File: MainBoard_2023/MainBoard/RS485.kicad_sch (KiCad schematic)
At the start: 26 parts, among them J8 43223-6113, U10 LTC1480CN8#PBF, U11 MAX3485, U12 LTC1480CN8#PBF, U13 MAX3485, U14 LTC1480CN8#PBF, U8 MAX3485, U9 TC7S14F

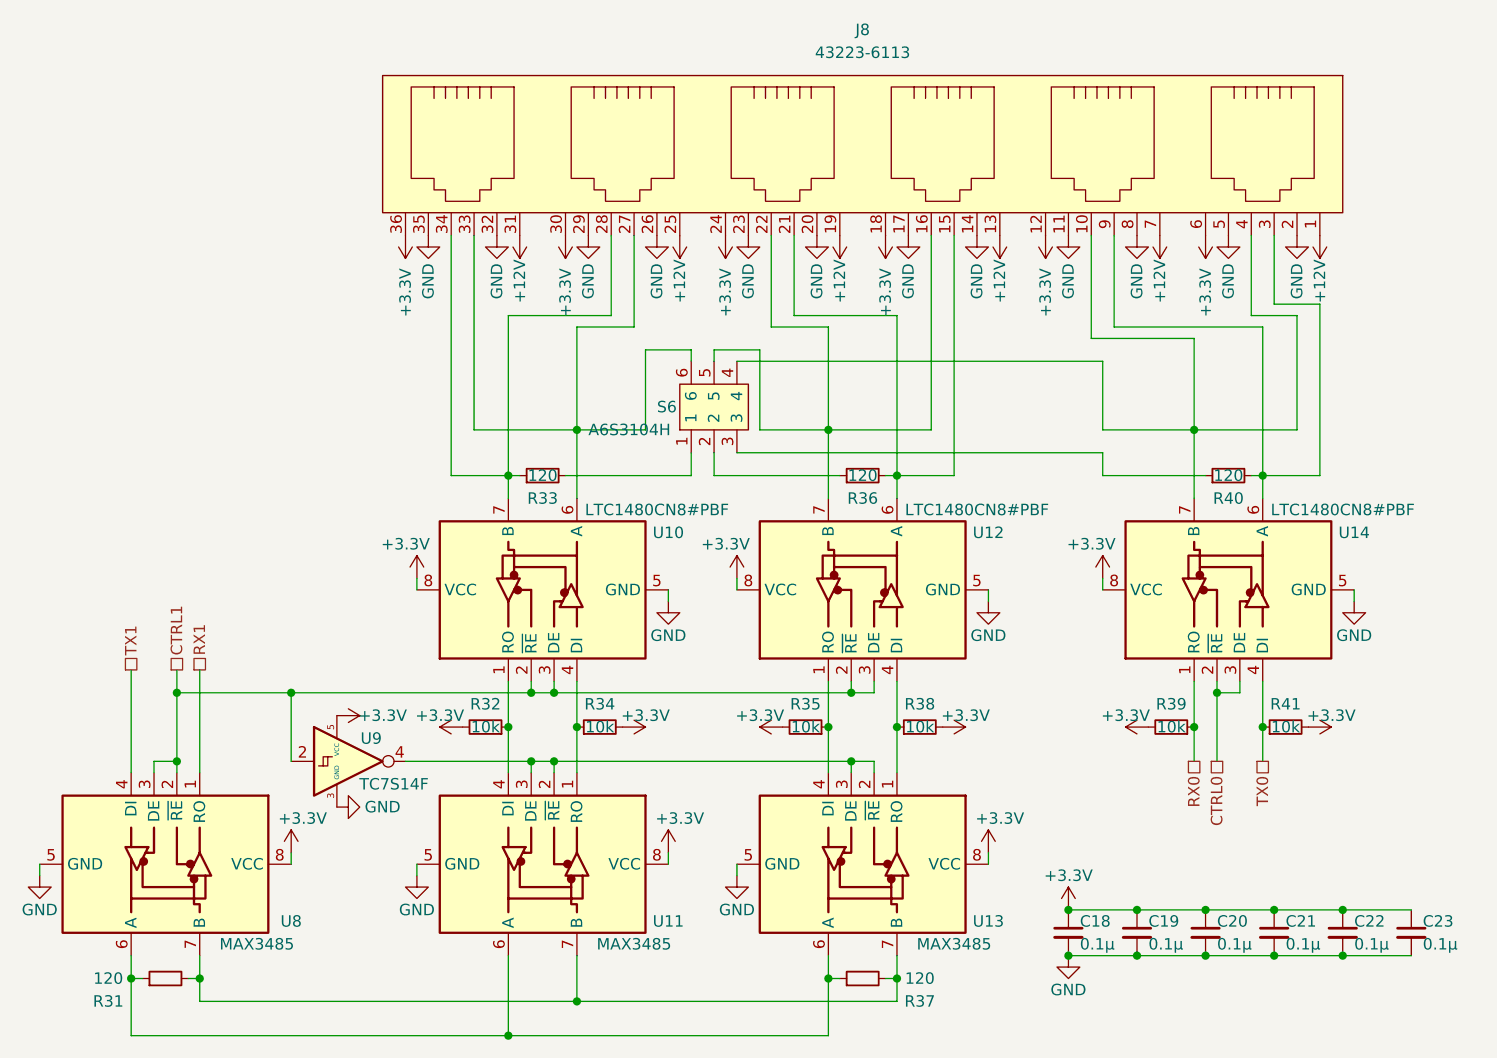
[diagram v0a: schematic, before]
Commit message: 配線
ICP10111の穴をNPTHに変更
RJ11の12Vと3V3を逆に
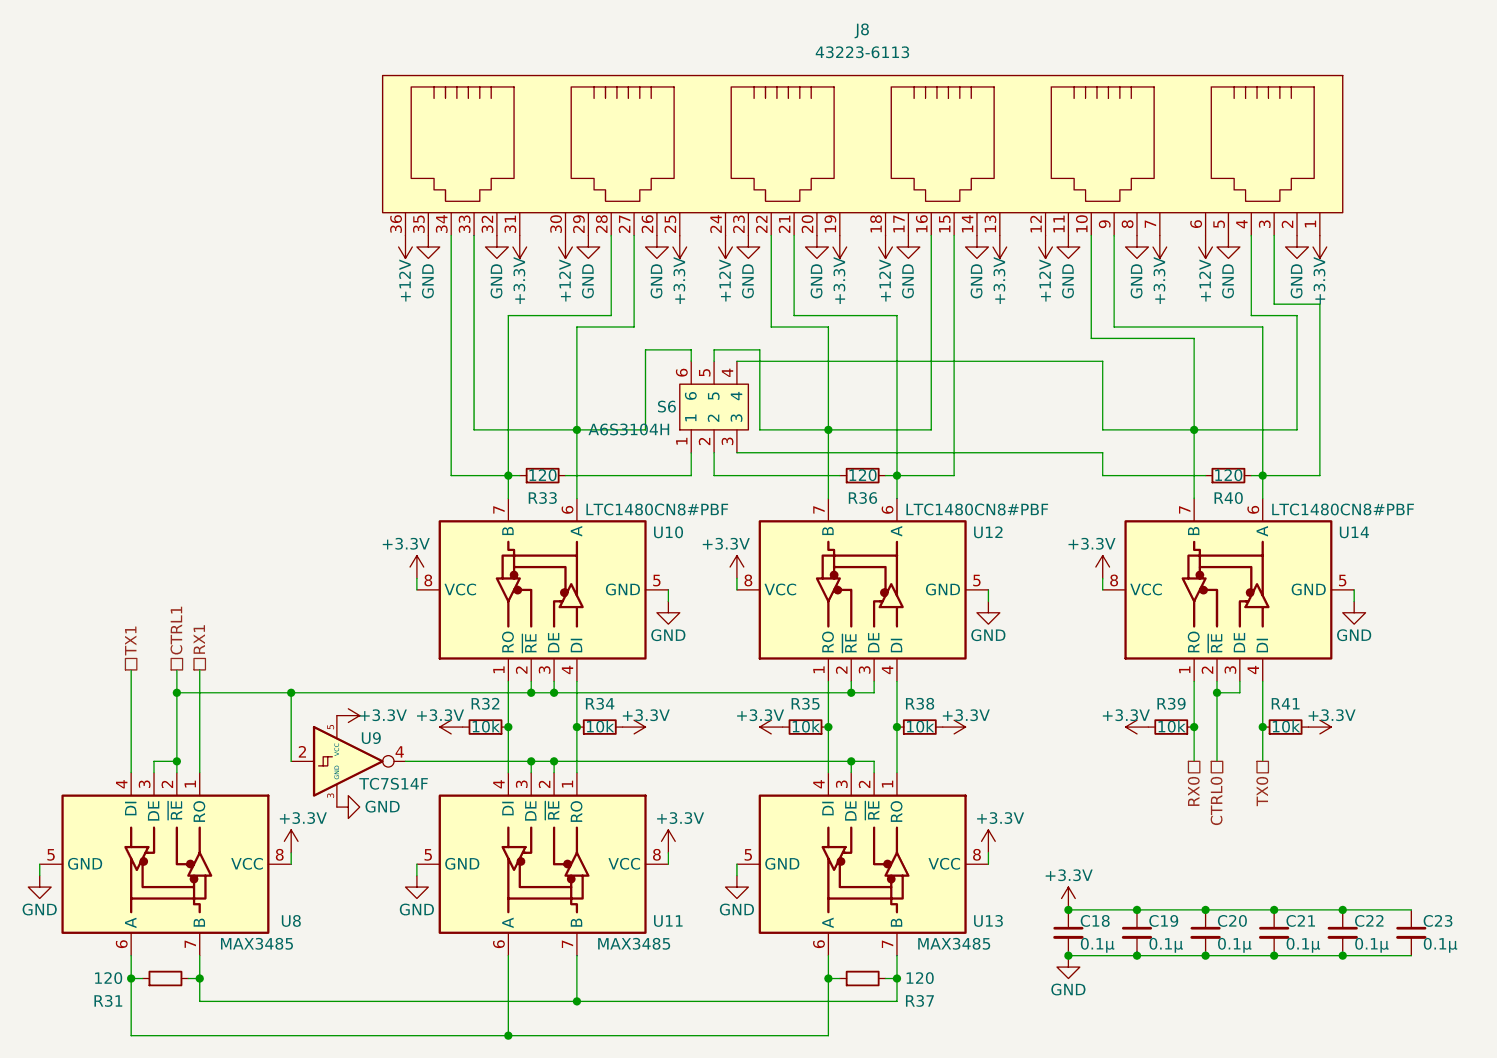
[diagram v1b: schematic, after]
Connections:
- net +12V: now also J8.12, J8.18, J8.24, J8.30, J8.36, J8.6; no longer J8.1, J8.13, J8.19, J8.25, J8.31, J8.7
- net +3.3V: now also J8.1, J8.13, J8.19, J8.25, J8.31, J8.7; no longer J8.12, J8.18, J8.24, J8.30, J8.36, J8.6
